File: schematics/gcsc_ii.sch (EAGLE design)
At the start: 41 parts, among them IC1 LM2574N-2-5.0, IC2 LTV-816, IC3 PIC12C508JN, J1 MAST, J2 POWER, J3 IC3_1-4, J4 IC3_5-8, J5 EXT, Q1 NTD4906N-35G, Q2 NTD4906N-35G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

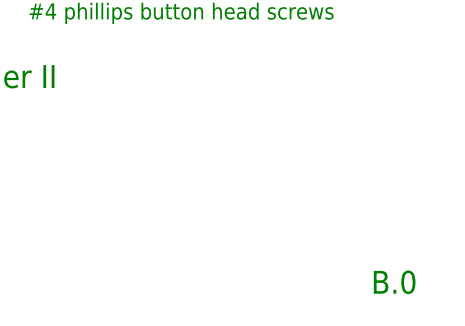
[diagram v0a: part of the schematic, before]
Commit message: Cleaned-up silk screen and some minor clean-up to traces.
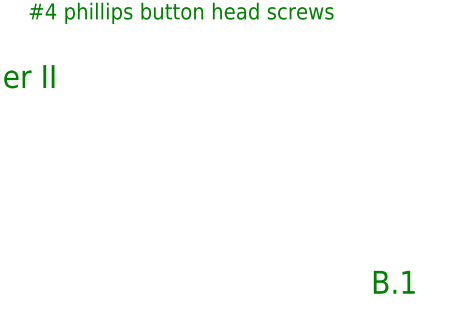
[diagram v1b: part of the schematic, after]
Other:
- note added: "B.1"
- note removed: "B.0"
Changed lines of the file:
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@@
 <?xml version="1.0" encoding="utf-8"?>
 <!DOCTYPE eagle SYSTEM "eagle.dtd">
-<eagle version="6.2">
+<eagle version="6.5.0">
 <drawing>
 <settings>
@@
 <text x="149.86" y="50.8" size="2.54" layer="91">Output Stage</text>
 <text x="17.78" y="15.24" size="2.54" layer="91">ICSP(PicKit3) Connector (optional)</text>
-<text x="238.76" y="7.62" size="2.54" layer="91" ratio="10">B.0</text>
+<text x="238.76" y="7.62" size="2.54" layer="91" ratio="10">B.1</text>
 <text x="149.86" y="25.4" size="1.778" layer="91">Kevin M. Fodor</text>
 <text x="78.74" y="40.64" size="1.778" layer="91">Breakout Jumpers</text>

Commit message: Cleaned-up silkscreen, thickened traces. Electrically design is unaltered
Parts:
- BELL.OUT, ICSP, J3, J4, LAMP1.OUT, LAMP2.OUT, TRIGGER.IN: BOM (none) -> EXCLUDE
- J5: BOM (none) -> INCLUDE; DNP (none) -> F
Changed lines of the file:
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@@
 <schematic xreflabel="%F%N/%S.%C%R" xrefpart="/%S.%C%R">
 <attributes>
+<attribute name="DATABASE" value="C:\projects\common\EagleCad\ulp\PARTSDB.txt"/>
 </attributes>
 <variantdefs>
@@
 <part name="GND3" library="supply1" deviceset="GND" device=""/>
 <part name="J5" library="kevin" deviceset="M03" device="POLAR_LOCK" value="EXT">
+<attribute name="BOM" value="INCLUDE"/>
+<attribute name="DNP" value="F"/>
 <attribute name="PARTNO" value="22-27-2031"/>
 </part>
 <part name="GND4" library="supply1" deviceset="GND" device=""/>
 <part name="J3" library="kevin" deviceset="M04" device="LOCK" value="IC3_1-4">
+<attribute name="BOM" value="EXCLUDE"/>
 <attribute name="DNP" value="T"/>
 <attribute name="PARTNO" value="22-28-4042"/>
 </part>
 <part name="J4" library="kevin" deviceset="M04" device="LOCK" value="IC3_5-8">
+<attribute name="BOM" value="EXCLUDE"/>
 <attribute name="DNP" value="T"/>
 <attribute name="PARTNO" value="22-28-4042"/>
@@
 </part>
 <part name="LAMP2.OUT" library="kevin" deviceset="LSP10" device="" value="LAMP2">
+<attribute name="BOM" value="EXCLUDE"/>
 <attribute name="DNP" value="T"/>
 <attribute name="PARTNO" value="22-28-4012"/>
 </part>
 <part name="LAMP1.OUT" library="kevin" deviceset="LSP10" device="" value="LAMP1">
+<attribute name="BOM" value="EXCLUDE"/>
 <attribute name="DNP" value="T"/>
 <attribute name="PARTNO" value="22-28-4012"/>
 </part>
 <part name="TRIGGER.IN" library="kevin" deviceset="LSP10" device="" value="TRIGGER">
+<attribute name="BOM" value="EXCLUDE"/>
 <attribute name="DNP" value="T"/>
 <attribute name="PARTNO" value="22-28-4012"/>
 </part>
 <part name="BELL.OUT" library="kevin" deviceset="LSP10" device="" value="BELL">
+<attribute name="BOM" value="EXCLUDE"/>
 <attribute name="DNP" value="T"/>
 <attribute name="PARTNO" value="22-28-4012"/>
@@
 <part name="P+6" library="supply1" deviceset="+5V" device=""/>
 <part name="ICSP" library="kevin" deviceset="PIC_ICSP" device="_RA">
+<attribute name="BOM" value="EXCLUDE"/>
 <attribute name="DNP" value="T"/>
 <attribute name="PARTNO" value="68016-106HLF"/>
@@
 <instance part="J5" gate="G$1" x="116.84" y="35.56">
 <attribute name="PARTNO" x="116.84" y="35.56" size="1.778" layer="96" display="off"/>
+<attribute name="BOM" x="116.84" y="35.56" size="1.778" layer="96" display="off"/>
+<attribute name="DNP" x="116.84" y="35.56" size="1.778" layer="96" display="off"/>
 </instance>
 <instance part="GND4" gate="1" x="127" y="27.94" rot="MR0"/>
@@
 <attribute name="DNP" x="78.74" y="58.42" size="1.778" layer="96" display="off"/>
 <attribute name="PARTNO" x="78.74" y="58.42" size="1.778" layer="96" display="off"/>
+<attribute name="BOM" x="78.74" y="58.42" size="1.778" layer="96" rot="R180" display="off"/>
 </instance>
 <instance part="J4" gate="G$1" x="68.58" y="38.1" smashed="yes" rot="MR0">
 <attribute name="DNP" x="68.58" y="38.1" size="1.778" layer="96" display="off"/>
 <attribute name="PARTNO" x="68.58" y="38.1" size="1.778" layer="96" display="off"/>
+<attribute name="BOM" x="68.58" y="38.1" size="1.778" layer="96" rot="MR0" display="off"/>
 </instance>
 <instance part="GP5" gate="G$1" x="76.2" y="101.6" smashed="yes">
@@
 <attribute name="DNP" x="86.36" y="101.6" size="1.778" layer="96" display="off"/>
 <attribute name="PARTNO" x="86.36" y="101.6" size="1.778" layer="96" display="off"/>
+<attribute name="BOM" x="86.36" y="101.6" size="1.778" layer="96" rot="R270" display="off"/>
 </instance>
 <instance part="LAMP1.OUT" gate="1" x="86.36" y="99.06" smashed="yes" rot="R270">
 <attribute name="DNP" x="86.36" y="99.06" size="1.778" layer="96" display="off"/>
 <attribute name="PARTNO" x="86.36" y="99.06" size="1.778" layer="96" display="off"/>
+<attribute name="BOM" x="86.36" y="99.06" size="1.778" layer="96" rot="R270" display="off"/>
 </instance>
 <instance part="TRIGGER.IN" gate="1" x="86.36" y="96.52" smashed="yes" rot="R270">
 <attribute name="DNP" x="86.36" y="96.52" size="1.778" layer="96" display="off"/>
 <attribute name="PARTNO" x="86.36" y="96.52" size="1.778" layer="96" display="off"/>
+<attribute name="BOM" x="86.36" y="96.52" size="1.778" layer="96" rot="R270" display="off"/>
 </instance>
 <instance part="BELL.OUT" gate="1" x="86.36" y="93.98" smashed="yes" rot="R270">
 <attribute name="DNP" x="86.36" y="93.98" size="1.778" layer="96" display="off"/>
 <attribute name="PARTNO" x="86.36" y="93.98" size="1.778" layer="96" display="off"/>
+<attribute name="BOM" x="86.36" y="93.98" size="1.778" layer="96" rot="R270" display="off"/>
 </instance>
 <instance part="GND2" gate="1" x="60.96" y="30.48"/>
@@
 <attribute name="DNP" x="17.78" y="27.94" size="1.778" layer="96" display="off"/>
 <attribute name="PARTNO" x="17.78" y="27.94" size="1.778" layer="96" display="off"/>
+<attribute name="BOM" x="17.78" y="27.94" size="1.778" layer="96" display="off"/>
 </instance>
 <instance part="J2" gate="G$1" x="15.24" y="160.02">

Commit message: Updated PCB to Rev B.1 No changes to parts or design. Only some cleaning up of traces (thickening) and cosmetic improvements
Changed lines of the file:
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@@
 <layer number="110" name="fp0" color="7" fill="1" visible="no" active="yes"/>
 <layer number="111" name="LPC17xx" color="7" fill="1" visible="yes" active="yes"/>
+<layer number="112" name="bGTest" color="1" fill="1" visible="no" active="no"/>
+<layer number="113" name="IDFDebug" color="7" fill="1" visible="yes" active="yes"/>
 <layer number="116" name="Patch_BOT" color="9" fill="4" visible="no" active="yes"/>
 <layer number="121" name="_tsilk" color="7" fill="1" visible="no" active="yes"/>
@@
 <layer number="124" name="bTestmark" color="7" fill="1" visible="no" active="yes"/>
 <layer number="125" name="_tNames" color="7" fill="1" visible="no" active="yes"/>
+<layer number="126" name="_bNames" color="7" fill="1" visible="yes" active="yes"/>
+<layer number="127" name="_tValues" color="7" fill="1" visible="yes" active="yes"/>
+<layer number="128" name="_bValues" color="7" fill="1" visible="yes" active="yes"/>
 <layer number="131" name="tAdjust" color="7" fill="1" visible="no" active="yes"/>
 <layer number="132" name="bAdjust" color="7" fill="1" visible="no" active="yes"/>
 <layer number="144" name="Drill_legend" color="7" fill="1" visible="no" active="yes"/>
+<layer number="150" name="Notes" color="7" fill="1" visible="yes" active="yes"/>
 <layer number="151" name="HeatSink" color="7" fill="1" visible="no" active="yes"/>
+<layer number="152" name="_bDocu" color="7" fill="1" visible="yes" active="yes"/>
 <layer number="199" name="Contour" color="7" fill="1" visible="yes" active="yes"/>
 <layer number="200" name="200bmp" color="1" fill="10" visible="no" active="no"/>
@@
 <layer number="223" name="223bmp" color="24" fill="1" visible="no" active="no"/>
 <layer number="224" name="224bmp" color="25" fill="1" visible="no" active="no"/>
+<layer number="231" name="Eagle3D_PG1" color="7" fill="1" visible="yes" active="yes"/>
+<layer number="232" name="Eagle3D_PG2" color="7" fill="1" visible="yes" active="yes"/>
+<layer number="233" name="Eagle3D_PG3" color="7" fill="1" visible="yes" active="yes"/>
+<layer number="248" name="Housing" color="7" fill="1" visible="yes" active="yes"/>
+<layer number="249" name="Edge" color="7" fill="1" visible="yes" active="yes"/>
 <layer number="250" name="Descript" color="3" fill="1" visible="no" active="no"/>
 <layer number="251" name="SMDround" color="12" fill="11" visible="no" active="no"/>

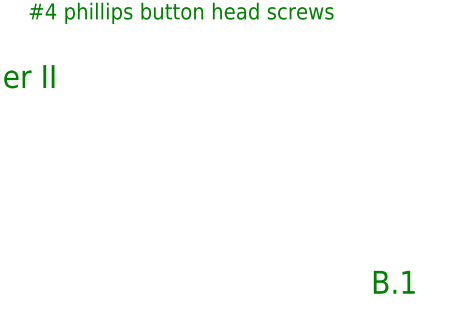
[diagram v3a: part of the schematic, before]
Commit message: Made slight modification to the top-silk to add heavier font for the "+" markings on the LEDs. Also updated to Eagle 6.6.0. Regenerated gerbers, schematic and archive.
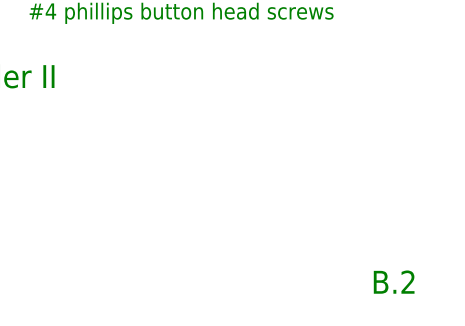
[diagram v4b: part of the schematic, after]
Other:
- note added: "B.2"
- note removed: "B.1"
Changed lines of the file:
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@@
 <?xml version="1.0" encoding="utf-8"?>
 <!DOCTYPE eagle SYSTEM "eagle.dtd">
-<eagle version="6.5.0">
+<eagle version="6.6.0">
 <drawing>
 <settings>
@@
 <text x="149.86" y="50.8" size="2.54" layer="91">Output Stage</text>
 <text x="17.78" y="15.24" size="2.54" layer="91">ICSP(PicKit3) Connector (optional)</text>
-<text x="238.76" y="7.62" size="2.54" layer="91" ratio="10">B.1</text>
+<text x="238.76" y="7.62" size="2.54" layer="91" ratio="10">B.2</text>
 <text x="149.86" y="25.4" size="1.778" layer="91">Kevin M. Fodor</text>
 <text x="78.74" y="40.64" size="1.778" layer="91">Breakout Jumpers</text>
